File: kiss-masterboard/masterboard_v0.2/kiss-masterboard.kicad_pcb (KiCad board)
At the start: 2 copper layers, 187 x 152 mm, 163 parts, among them J1 Cubebatt_host, J10 CRESET, J11 Jumper, J12 Jumper, J13 Conn_02x08_Odd_Even, J14 Conn_02x08_Odd_Even, J15 jmp, J16 jmp, J17 gain_jumper, J18 Speaker, J2 Conn_01x02, J3 Conn_01x02, J4 Conn_01x02, J5 Conn_01x02, J6 Conn_01x02, J7 Conn_01x02, J8 Jumper, J9 jmp, P2 CONN_02X20, U1 TPS54327, U10 CSD86360Q5D, U12 1V2, U13 SN74LVC8T245, U14 W25Q, U15 MPU-9250, U16 ADS1000, U17 12MHz, U2 SN74LVC8T245, U3 3.3V, U4 ICE40UP5k-SG48, U5 SN74LVC8T245, U6 MAX98357, U7 SPH0645LM4H, U8 5V150W-DCDC, U9 TPS53819A

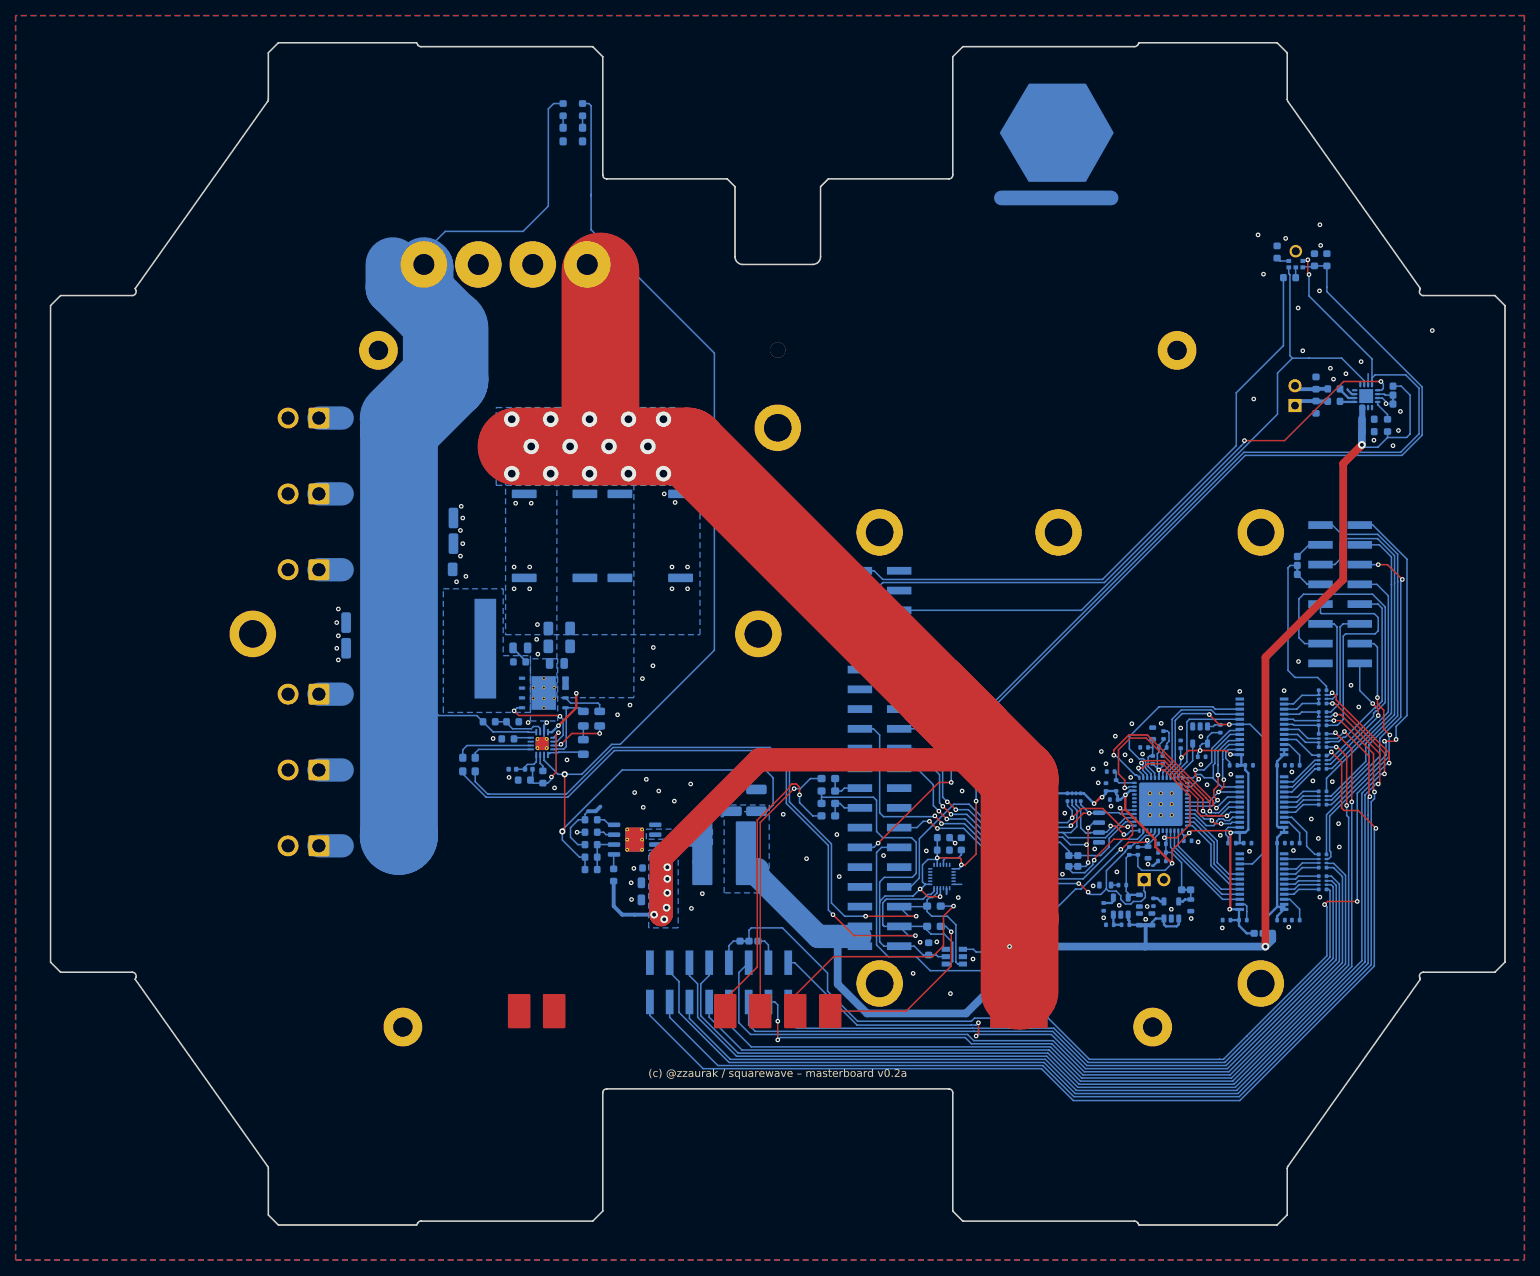
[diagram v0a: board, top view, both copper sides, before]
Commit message: wip: Added missing symbols, adjusted pcb layout
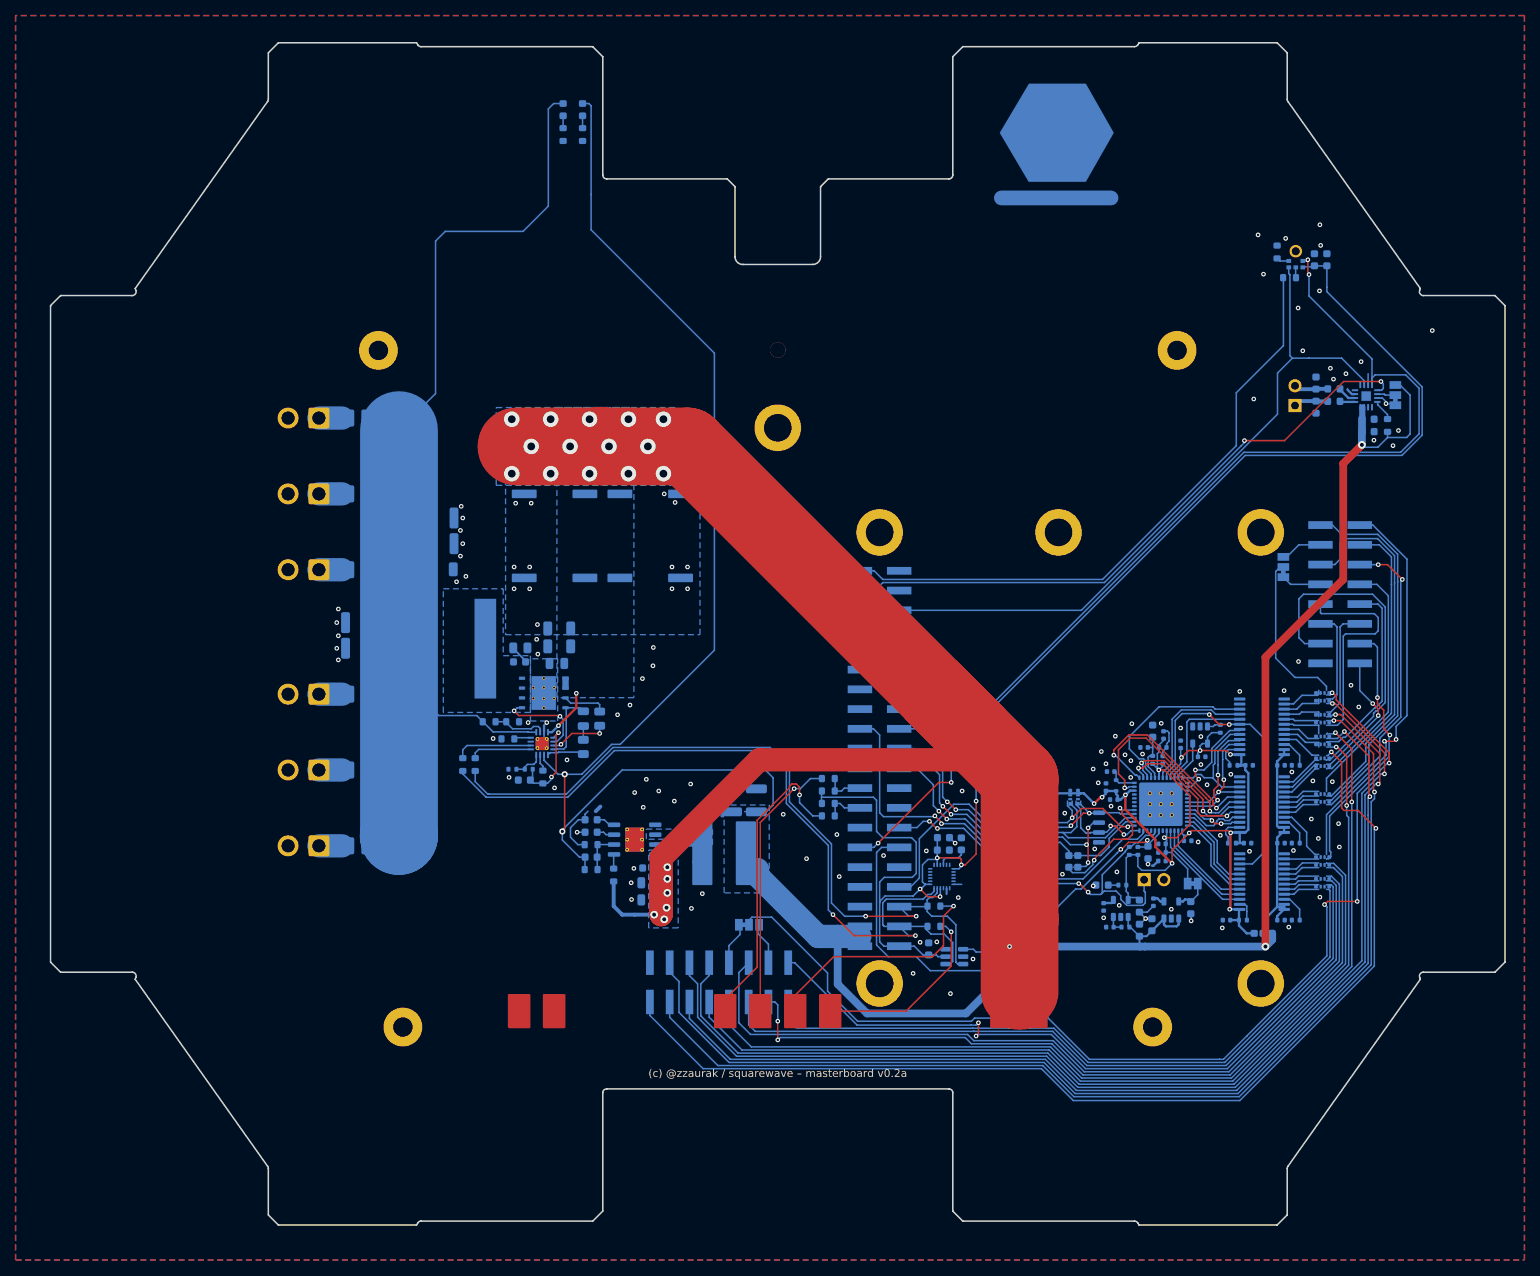
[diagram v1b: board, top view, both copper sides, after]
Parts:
- removed NT1: Net-Tie_2, NetTie:NetTie-2_SMD_Pad0.5mm
- removed U8: 5V150W-DCDC, kiss:150W5VDCDC
- C10: value 10u -> 10uF; footprint pkl_dipol:C_0603 -> Capacitor_SMD:C_0603_1608Metric
- C11, C12, C13, C14, C15, C16, C17, C19, C20, C21, C22, C24, C25, C27, C28, C29, C30, C31, C56, C57, C61, C8, C9: footprint pkl_dipol:C_0402 -> Capacitor_SMD:C_0402_1005Metric
- C18, C23, C26, C54: footprint pkl_dipol:C_0603 -> Capacitor_SMD:C_0603_1608Metric
- C35: value 1uF -> 1µF
- D5, D6: footprint pkl_dipol:D_0603 -> LED_SMD:LED_0603_1608Metric
- J15, J16, J17: footprint pkl_jumpers:J_NCNO_0903_30 -> Jumper:SolderJumper-3_P1.3mm_Bridged12_Pad1.0x1.5mm_NumberLabels
- J8: footprint pkl_jumpers:J_NC_0603_30 -> Jumper:SolderJumper-2_P1.3mm_Bridged_Pad1.0x1.5mm
- L2, L3, L4, L5, L6, L7: footprint Inductor_SMD:L_1206_3216Metric -> Inductor_SMD:L_1008_2520Metric
- R1, R2, R3, R31, R32, R4, R5, R6, R7, R8: footprint Resistor_SMD:R_0603_1608Metric_Pad1.05x0.95mm_HandSolder -> Resistor_SMD:R_0603_1608Metric
- R14, R15, R16, R17, R20, R21, R22, R23, R24, R26, R27, R30: footprint pkl_dipol:R_0402 -> Resistor_SMD:R_0402_1005Metric
- R33: value R -> 1M
- R9: value 10k -> 10K
- U6: footprint Package_DFN_QFN:QFN-16-1EP_3x3mm_P0.5mm_EP1.8x1.8mm -> Package_DFN_QFN:TQFN-16-1EP_3x3mm_P0.5mm_EP1.23x1.23mm
- moved J15 2.10 mm to (104.3, 126.9)
- moved J16 1.81 mm to (173.0, 80.9)
- moved C18 1.40 mm to (154.5, 127.6)
- moved J8 1.17 mm to (161.3, 121.6)
- moved C23 0.70 mm to (154.5, 124.5)
- moved C26 0.70 mm to (156.1, 126.9)
- moved D5 0.40 mm to (149.7, 121.8)
- moved J17 0.30 mm to (187.4, 58.8)
- moved C10 0.30 mm to (156.2, 102.0)
- moved C14 0.30 mm to (150.7, 127.2)
- moved C54 0.30 mm to (161.1, 124.7)
- moved R16 0.30 mm to (152.7, 127.2)
- moved U3 0.30 mm to (152.1, 124.8)
- moved J12 0.10 mm to (146.0, 119.5)
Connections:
- net /Digital Audio/3V3 renamed /Raspberry Pi/3v3
- net /FPGA Panel Driver/CRESET renamed /FPGA Panel Driver/iCE_CRESET
- net /FPGA Panel Driver/FLASH_~HLD~|~RST~|IO3 renamed /FPGA Panel Driver/FLASH_~{HLD}|~{RST}|IO3
- net /FPGA Panel Driver/FLASH_~WP~|IO2 renamed /FPGA Panel Driver/FLASH_~{WP}|IO2
- net /FPGA Panel Driver/MISO renamed /FPGA Panel Driver/FLASH_MISO|IO1
- net /FPGA Panel Driver/MOSI renamed /FPGA Panel Driver/FLASH_MOSI|IO0
- net /FPGA Panel Driver/SCK renamed /FPGA Panel Driver/iCE_SCK
- net /Raspberry Pi/FPGA_FLASH_SS renamed /FPGA Panel Driver/iCE_SS_B
- net /Raspberry Pi/FPGA_SS renamed /FPGA Panel Driver/FPGA_SS_PANEL
- C4 pad 2: GNDA -> GND
- P2 pad 10: Net-(P2-Pad10) -> unconnected-(P2-P10-Pad10)
- P2 pad 11: /FPGA Panel Driver/CDONE -> /FPGA Panel Driver/iCE_CDONE
- P2 pad 15: Net-(P2-Pad15) -> unconnected-(P2-P15-Pad15)
- P2 pad 17: Net-(P2-Pad17) -> unconnected-(P2-P17-Pad17)
- P2 pad 22: Net-(P2-Pad22) -> unconnected-(P2-P22-Pad22)
- P2 pad 26: Net-(P2-Pad26) -> unconnected-(P2-P26-Pad26)
- P2 pad 27: Net-(P2-Pad27) -> unconnected-(P2-P27-Pad27)
- P2 pad 28: Net-(P2-Pad28) -> unconnected-(P2-P28-Pad28)
- P2 pad 29: Net-(P2-Pad29) -> unconnected-(P2-P29-Pad29)
- P2 pad 31: Net-(P2-Pad31) -> unconnected-(P2-P31-Pad31)
- P2 pad 32: Net-(P2-Pad32) -> unconnected-(P2-P32-Pad32)
- P2 pad 33: Net-(P2-Pad33) -> unconnected-(P2-P33-Pad33)
- P2 pad 36: Net-(P2-Pad36) -> unconnected-(P2-P36-Pad36)
- P2 pad 37: Net-(P2-Pad37) -> unconnected-(P2-P37-Pad37)
- P2 pad 8: Net-(P2-Pad8) -> unconnected-(P2-P8-Pad8)
- R11 pad 1: GNDA -> GND
- R20 pad 2: Net-(D5-PadA) -> Net-(D5-A)
- R24 pad 2: /FPGA Panel Driver/CDONE -> /FPGA Panel Driver/iCE_CDONE
- U15 pad 11: Net-(U15-Pad11) -> unconnected-(U15-FSYNC-Pad11)
- U15 pad 12: Net-(U15-Pad12) -> unconnected-(U15-INT-Pad12)
- U15 pad 21: Net-(U15-Pad21) -> unconnected-(U15-AUX_DA-Pad21)
- U15 pad 7: Net-(U15-Pad7) -> unconnected-(U15-AUX_CL-Pad7)
- U15 pad 9: Net-(U15-Pad9) -> unconnected-(U15-AD0/MISO-Pad9)
- U17 pad 2: Net-(U17-Pad2) -> unconnected-(U17-NC-Pad2)
- U2 pad 15: Net-(U2-Pad15) -> unconnected-(U2-B6-Pad15)
- U2 pad 9: Net-(U2-Pad9) -> unconnected-(U2-A6-Pad9)
- U4 pad 10: Net-(U4-Pad10) -> unconnected-(U4-IOB_18A-Pad10)
- U4 pad 18: Net-(U4-Pad18) -> unconnected-(U4-IOB_31B-Pad18)
- U4 pad 19: Net-(U4-Pad19) -> unconnected-(U4-IOB_29B-Pad19)
- U4 pad 20: Net-(U4-Pad20) -> unconnected-(U4-IOB_25B_G3-Pad20)
- U4 pad 21: Net-(U4-Pad21) -> unconnected-(U4-IOB_23B-Pad21)
- U4 pad 37: Net-(U4-Pad37) -> unconnected-(U4-IOT_45A_G1-Pad37)
- U4 pad 39: Net-(U4-Pad39) -> unconnected-(U4-RGB2-Pad39)
- U4 pad 40: Net-(U4-Pad40) -> unconnected-(U4-RGB1-Pad40)
- U4 pad 41: Net-(U4-Pad41) -> unconnected-(U4-RGB0-Pad41)
- U4 pad 7: /FPGA Panel Driver/CDONE -> /FPGA Panel Driver/iCE_CDONE
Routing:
- net /FPGA Panel Driver/iCE_CDONE: track 0.00 -> 62.7 mm, vias 0 -> 2
- net /FPGA Panel Driver/CDONE: track 62.7 -> 0.00 mm, vias 2 -> 0
- net /Panel_power: track 150.0 -> 124.2 mm
- net /Power_switched: track 219.5 -> 197.1 mm
- net GND: track 18.2 -> 31.6 mm, vias 131 -> 129
- net GNDA: track 7.03 -> 0.00 mm
- net Net-(J14-Pin_8): track 3.51 -> 5.16 mm
- net +1V2: track 2.91 -> 4.35 mm
- net Net-(J14-Pin_4): track 3.60 -> 4.90 mm
- net /FPGA Panel Driver/iCE_CRESET: track 51.0 -> 52.0 mm
- net /FPGA Panel Driver/P1_A4x: track 133.7 -> 134.7 mm
- net Net-(J13-Pin_4): track 3.83 -> 4.83 mm
- net Net-(J13-Pin_8): track 3.87 -> 4.87 mm
- net Net-(D5-PadA): track 0.95 -> 0.00 mm
- net Net-(D5-A): track 0.00 -> 0.95 mm
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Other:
- outline, holes or cut-outs redrawn
- net class Default removed

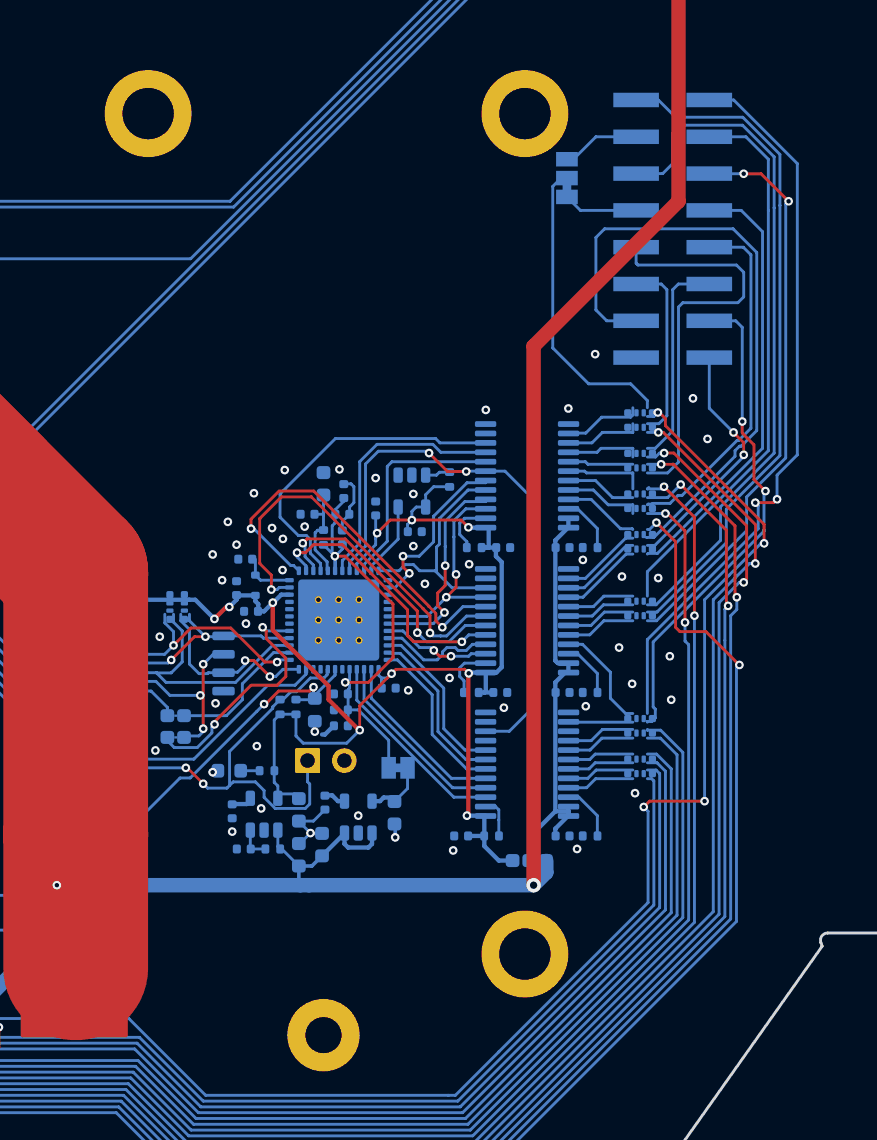
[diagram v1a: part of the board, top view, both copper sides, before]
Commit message: replaced resistor array with normal resistors
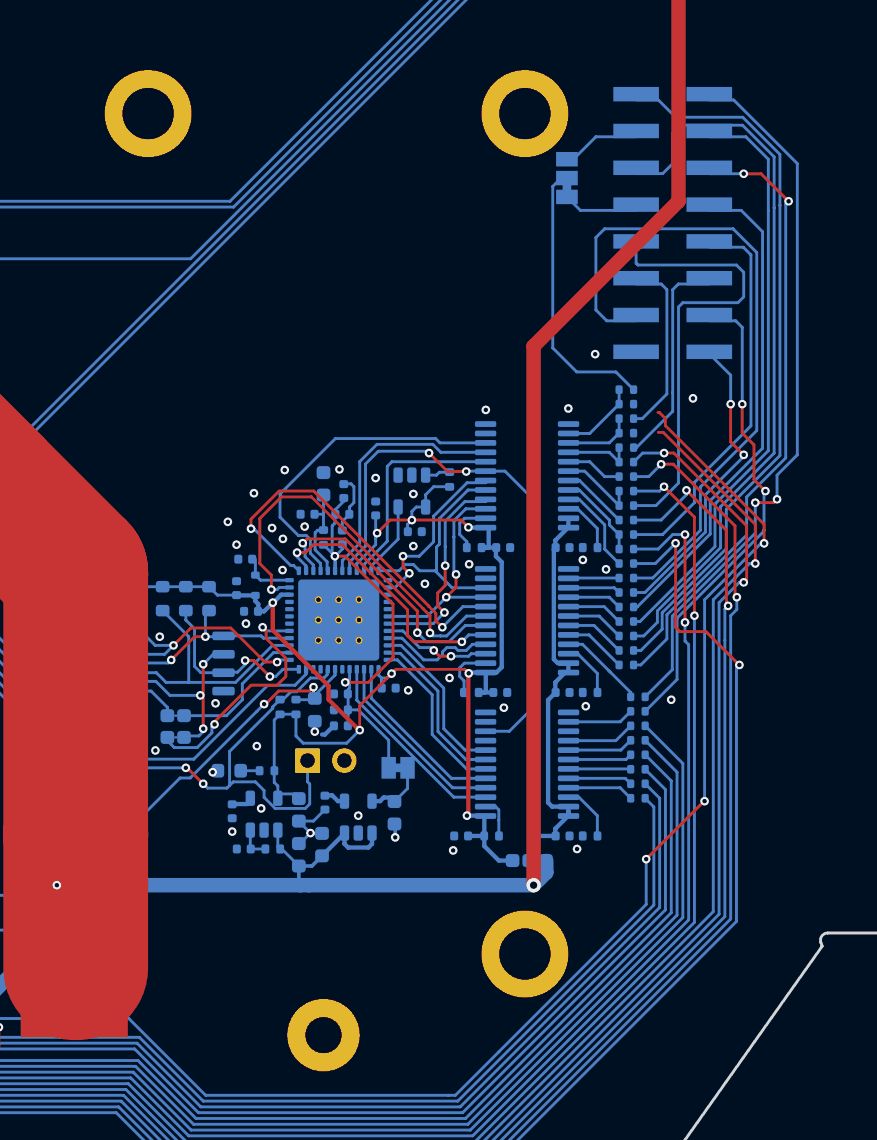
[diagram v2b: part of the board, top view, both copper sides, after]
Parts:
- removed R12, R13, R18, R19, R25, R28, R29: 33E, pkl_dipol:R_Array_Convex_4x0402
- added R45: 10k, Resistor_SMD:R_0603_1608Metric, B.Cu at (148.3, 109.9)
- added R47: 10k, Resistor_SMD:R_0603_1608Metric, B.Cu at (146.7, 109.9)
- added R48: 10k, Resistor_SMD:R_0603_1608Metric, B.Cu at (143.5, 109.9)
- added R51: 2-2.2M (33E), pkl_dipol:R_0402, B.Cu at (177.1, 107.5)
- added R52: 2-2.2M (33E), pkl_dipol:R_0402, B.Cu at (177.1, 104.5)
- added R53: 2-2.2M (33E), pkl_dipol:R_0402, B.Cu at (177.1, 101.5)
- added R54: 2-2.2M (33E), pkl_dipol:R_0402, B.Cu at (177.1, 106.5)
- added R55: 2-2.2M (33E), pkl_dipol:R_0402, B.Cu at (177.1, 105.5)
- added R56: 2-2.2M (33E), pkl_dipol:R_0402, B.Cu at (177.1, 102.5)
- added R57: 2-2.2M (33E), pkl_dipol:R_0402, B.Cu at (177.1, 103.5)
- added R58: 2-2.2M (33E), pkl_dipol:R_0402, B.Cu at (177.1, 100.5)
- added R59: 2-2.2M (33E), pkl_dipol:R_0402, B.Cu at (177.1, 99.5)
- added R60: 2-2.2M (33E), pkl_dipol:R_0402, B.Cu at (177.1, 98.5)
- added R61: 2-2.2M (33E), pkl_dipol:R_0402, B.Cu at (177.1, 97.5)
- added R62: 2-2.2M (33E), pkl_dipol:R_0402, B.Cu at (177.1, 96.5)
- added R63: 2-2.2M (33E), pkl_dipol:R_0402, B.Cu at (177.1, 95.5)
- added R64: 2-2.2M (33E), pkl_dipol:R_0402, B.Cu at (177.9, 116.7)
- added R65: 2-2.2M (33E), pkl_dipol:R_0402, B.Cu at (177.1, 114.5)
- added R66: 2-2.2M (33E), pkl_dipol:R_0402, B.Cu at (177.1, 113.5)
- added R67: 2-2.2M (33E), pkl_dipol:R_0402, B.Cu at (177.1, 112.5)
- added R68: 2-2.2M (33E), pkl_dipol:R_0402, B.Cu at (177.1, 111.5)
- added R69: 2-2.2M (33E), pkl_dipol:R_0402, B.Cu at (177.1, 110.5)
- added R70: 2-2.2M (33E), pkl_dipol:R_0402, B.Cu at (177.1, 109.5)
- added R71: 2-2.2M (33E), pkl_dipol:R_0402, B.Cu at (177.1, 108.5)
- added R72: 2-2.2M (33E), pkl_dipol:R_0402, B.Cu at (177.9, 123.7)
- added R73: 2-2.2M (33E), pkl_dipol:R_0402, B.Cu at (177.9, 122.7)
- added R74: 2-2.2M (33E), pkl_dipol:R_0402, B.Cu at (177.9, 121.7)
- added R75: 2-2.2M (33E), pkl_dipol:R_0402, B.Cu at (177.9, 120.7)
- added R76: 2-2.2M (33E), pkl_dipol:R_0402, B.Cu at (177.9, 119.7)
- added R77: 2-2.2M (33E), pkl_dipol:R_0402, B.Cu at (177.9, 118.7)
- added R78: 2-2.2M (33E), pkl_dipol:R_0402, B.Cu at (177.9, 117.7)
- C56: footprint Capacitor_SMD:C_0402_1005Metric -> Capacitor_SMD:C_0603_1608Metric
- R46: footprint pkl_dipol:R_Array_Convex_4x0402 -> Resistor_SMD:R_0603_1608Metric
- moved C56 2.12 mm to (141.1, 110.7), turned to 180 degrees
- moved R46 1.15 mm to (145.1, 109.9)
- moved J14 0.40 mm to (180.3, 84.0)
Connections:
- R46 pad 2: /FPGA Panel Driver/FLASH_~{HLD}|~{RST}|IO3 -> /FPGA Panel Driver/iCE_SCK
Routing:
- net /FPGA Panel Driver/P2_BLANKx: track 17.0 -> 21.2 mm
- net /FPGA Panel Driver/P2_B1x: track 30.2 -> 34.1 mm
- net /FPGA Panel Driver/P2_LATCHx: track 43.3 -> 46.9 mm
- net /FPGA Panel Driver/P2_R1x: track 39.6 -> 43.0 mm
- net /FPGA Panel Driver/P1_A4x: track 134.7 -> 131.4 mm, vias 4 -> 3
- net /FPGA Panel Driver/P2_G0x: track 47.2 -> 50.2 mm
- net /FPGA Panel Driver/P2_A1x: track 28.4 -> 31.2 mm
- net /FPGA Panel Driver/P2_G1x: track 47.9 -> 50.5 mm
- net /FPGA Panel Driver/P2_A0x: track 24.4 -> 26.9 mm
- net /FPGA Panel Driver/P2_B0x: track 38.3 -> 40.7 mm
- net Net-(U5-B7): track 5.60 -> 3.50 mm
- net Net-(U5-B6): track 5.66 -> 3.62 mm
- net /FPGA Panel Driver/P2_B1: track 5.68 -> 3.77 mm
- net /FPGA Panel Driver/P2_A4x: track 20.9 -> 19.1 mm
- net /FPGA Panel Driver/FLASH_~{HLD}|~{RST}|IO3: track 15.5 -> 17.3 mm
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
